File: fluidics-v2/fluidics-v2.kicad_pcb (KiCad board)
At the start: 4 copper layers, 127 x 127.2 mm, 73 parts, among them IC2 ADUM1250WSRZ-RL7, J1 PJ-063AH, J10 87832-1010, J11 0705430001, J12 87832-1010, J13 0705430001, J14 87832-1010, J15 0533980671, J16 0705430001, J17 0533980671, J18 87832-1010, J19 0705430001, J2 B6B-ZR-SM4-TF, J20 0533980671, J21 87832-1010, J22 0705430001, J24 0705430001, J25 87832-1010, J3 A-DS_15_A_KG-T4S, J4 B6B-ZR-SM4-TF, U10 LTC4311CSC6-TRPBF, U11 MAX3221, U12 CD4050BDR, U13 TC7PZ17FU, U2 Teensy4.1, U3 AP7366EA-33W5-7, U4 D24V10FX, U6 LTC4311CSC6-TRPBF, U8 LTC4311CSC6-TRPBF, U9 LTC4311CSC6-TRPBF

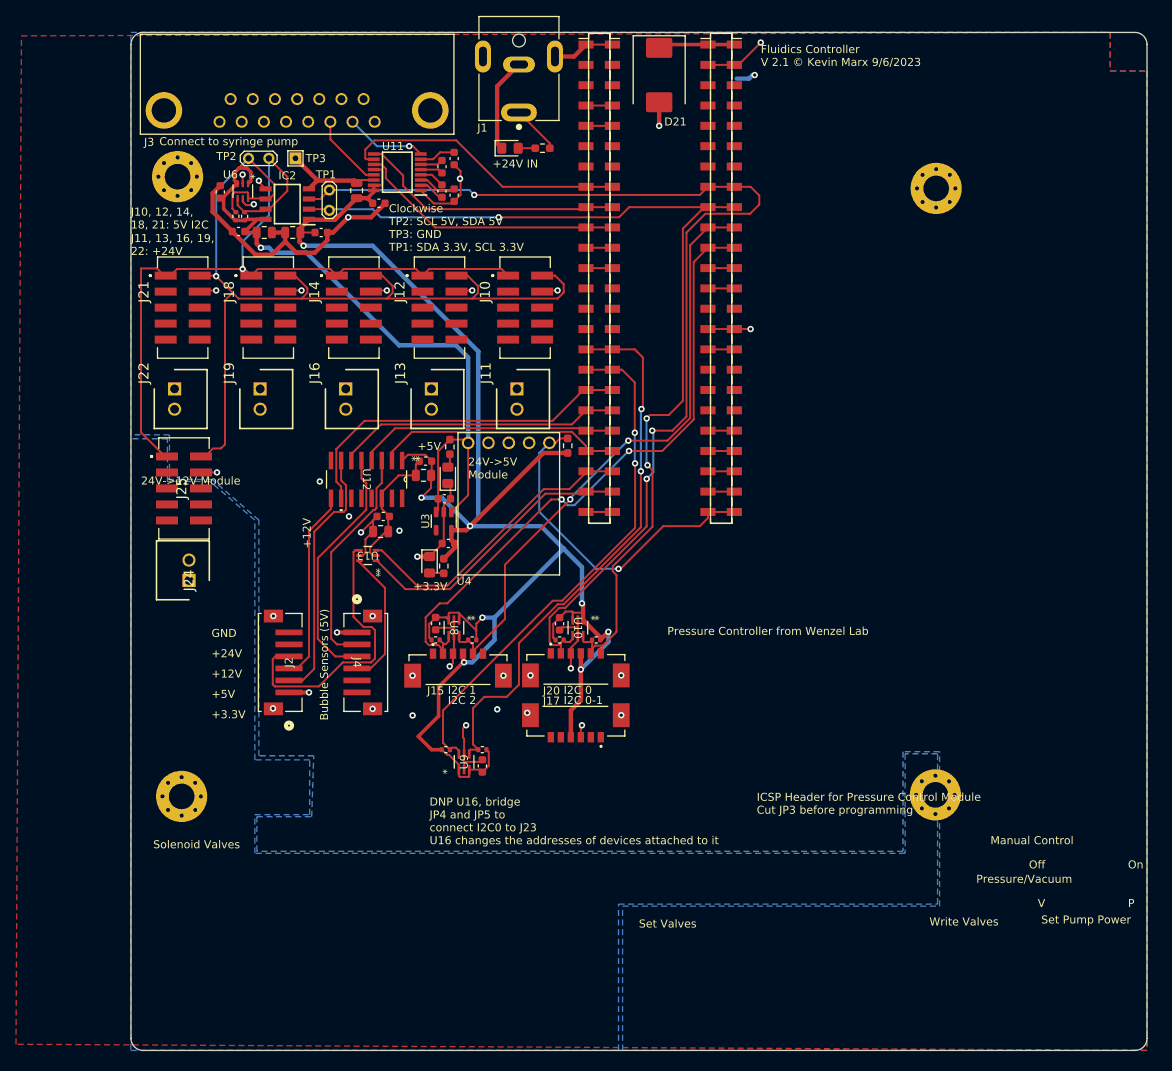
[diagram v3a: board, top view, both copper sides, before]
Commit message: @ Wire solenoid driver + status LEDs + I2C cleanup; route + connect
- Solenoid driver (U1 TPL7407): IN1-7 <- Teensy GPIO_1-7 (back-layer fanout,
  vias off the SMD pads), COM->+24V, GND->plane, OUT1-7 -> J5 screw terminal
- Add 7 solenoid status LEDs (GPIO_1-7) + COM/+24V indicator LED (0402)
- Remove LTC4311 I2C accelerators (U9/U10) - misbehaved on lightly-loaded
  buses (single-valve failure); kept passive pull-ups. Restored SCL2/SDA2
  pull-ups (R41/R42)
- Back layer: full-board GND pour (clean rectangle outline)
- Connect U1 GND and R4 (+24V power-indicator LED) to their nets

DRC: unconnected down to 5, all intentional unused-pin no-connects
(GPIO_8/9 + vestigial SPI). No shorts; vias cleared out of Teensy SMD pads.

Co-Authored-By: Claude Opus 4.8 (1M context) <noreply@anthropic.com>
@
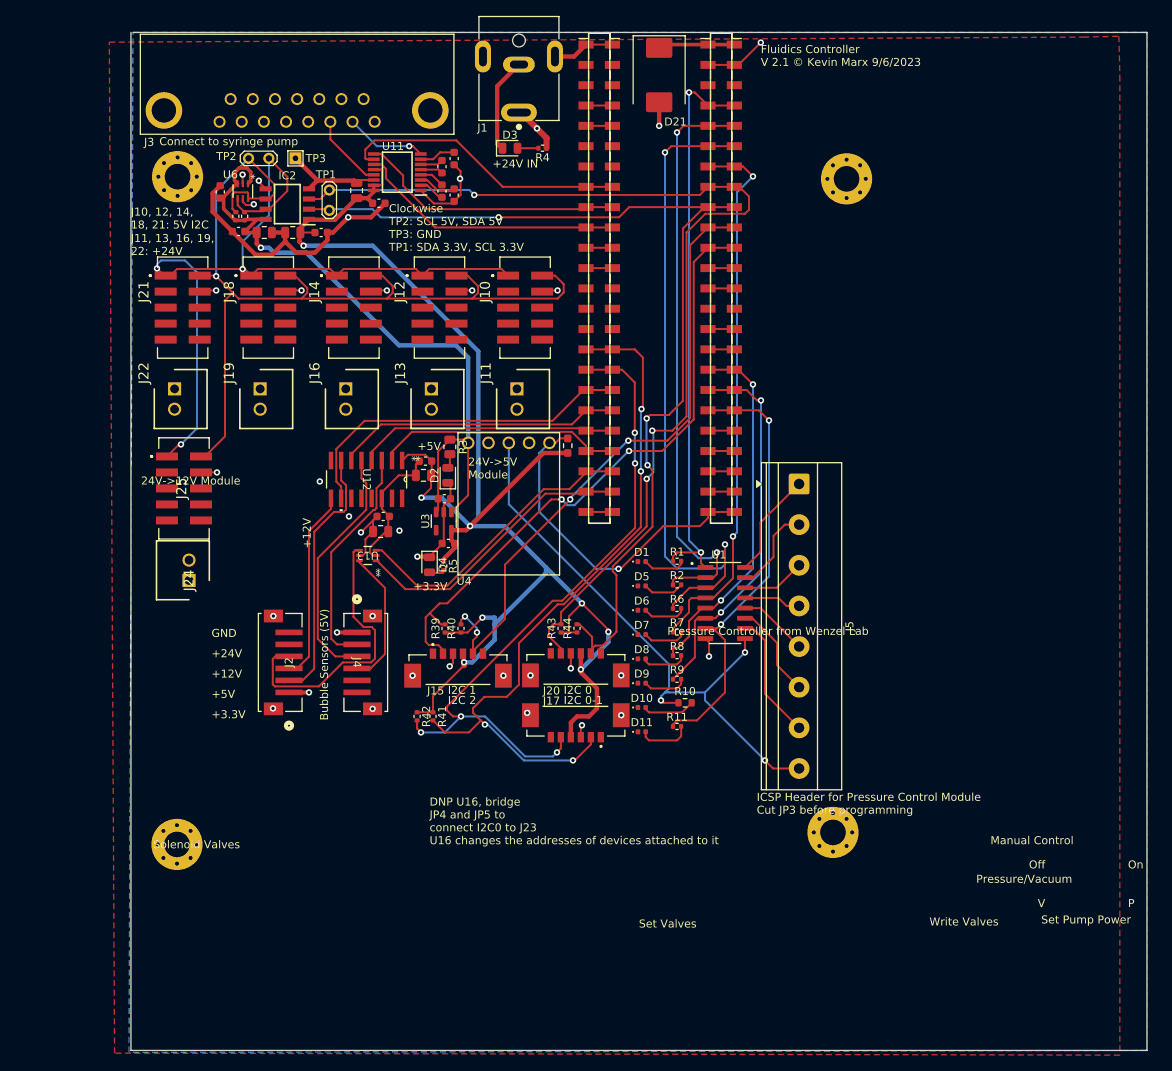
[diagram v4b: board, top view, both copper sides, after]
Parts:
- removed C12, C13, C14: 0.01u, Capacitor_SMD:C_0603_1608Metric
- removed U10, U8, U9: LTC4311CSC6-TRPBF, LTC:SOT-6_SC_LIT
- added D1: LED, LED_SMD:LED_0402_1005Metric, F.Cu at (78.6, 81.6)
- added D10: LED, LED_SMD:LED_0402_1005Metric, F.Cu at (78.6, 99.9)
- added D11: LED, LED_SMD:LED_0402_1005Metric, F.Cu at (78.6, 102.9)
- added D5: LED, LED_SMD:LED_0402_1005Metric, F.Cu at (78.6, 84.7)
- added D6: LED, LED_SMD:LED_0402_1005Metric, F.Cu at (78.6, 87.7)
- added D7: LED, LED_SMD:LED_0402_1005Metric, F.Cu at (78.6, 90.8)
- added D8: LED, LED_SMD:LED_0402_1005Metric, F.Cu at (78.6, 93.8)
- added D9: LED, LED_SMD:LED_0402_1005Metric, F.Cu at (78.6, 96.8)
- added J5: Screw_Terminal_01x08, TerminalBlock_Phoenix:TerminalBlock_Phoenix_MKDS-1,5-8-5.08_1x08_P5.08mm_Horizontal, F.Cu at (98.3, 71.9)
- added R1: 2.7K, Resistor_SMD:R_0402_1005Metric, F.Cu at (83.0, 81.6)
- added R10: 42K, Resistor_SMD:R_0603_1608Metric, F.Cu at (84.0, 99.3)
- added R11: 2.7K, Resistor_SMD:R_0402_1005Metric, F.Cu at (83.0, 102.2)
- added R2: 2.7K, Resistor_SMD:R_0402_1005Metric, F.Cu at (83.0, 84.5)
- added R6: 2.7K, Resistor_SMD:R_0402_1005Metric, F.Cu at (83.0, 87.5)
- added R7: 2.7K, Resistor_SMD:R_0402_1005Metric, F.Cu at (83.0, 90.5)
- added R8: 2.7K, Resistor_SMD:R_0402_1005Metric, F.Cu at (83.0, 93.4)
- added R9: 2.7K, Resistor_SMD:R_0402_1005Metric, F.Cu at (83.0, 96.3)
- added U1: TPL7407LDR, TPL7407LDR:SOIC127P600X175-16N, F.Cu at (89.0, 86.8)
- D2, D3, D4: footprint LED_SMD:LED_0805_2012Metric_Pad1.15x1.40mm_HandSolder -> LED_SMD:LED_0805_2012Metric
- R3: footprint Resistor_SMD:R_0603_1608Metric_Pad0.98x0.95mm_HandSolder -> Resistor_SMD:R_0805_2012Metric
- R4, R5: footprint Resistor_SMD:R_0603_1608Metric_Pad0.98x0.95mm_HandSolder -> Resistor_SMD:R_0402_1005Metric
- moved H3 13.6 mm to (102.5, 115.5)
- moved H1 11.3 mm to (104.2, 33.8)
- moved R41 7.45 mm to (52.5, 101.0), turned to -90 degrees
- moved H4 6.03 mm to (20.5, 117.0)
- moved R42 5.50 mm to (50.5, 101.0), turned to -90 degrees
- moved R44 2.80 mm to (70.5, 90.0), turned to 90 degrees
- moved R40 2.01 mm to (56.0, 90.0), turned to 90 degrees
- moved R39 1.86 mm to (54.0, 90.0), turned to 90 degrees
- moved R43 1.46 mm to (68.5, 90.0), turned to 90 degrees
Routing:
- net /GPIO_3: track 0.00 -> 82.7 mm, vias 0 -> 2
- net +24V: track 6.06 -> 79.6 mm, vias 0 -> 4
- net /GPIO_2: track 0.00 -> 73.5 mm, vias 0 -> 2
- net /GPIO_1: track 0.00 -> 70.9 mm, vias 0 -> 2
- net /GPIO_4: track 0.00 -> 68.8 mm, vias 0 -> 2
- net /GPIO_7: track 0.00 -> 56.3 mm, vias 0 -> 2
- net /GPIO_6: track 0.00 -> 47.9 mm, vias 0 -> 2
- net /GPIO_5: track 0.00 -> 46.4 mm, vias 0 -> 2
- net +3.3V: track 227.9 -> 194.5 mm
- net GND: track 160.0 -> 137.1 mm, vias 34 -> 30
- net /SCL2: track 68.9 -> 89.0 mm, vias 2 -> 4
- net /SDA2: track 65.1 -> 84.2 mm, vias 2 -> 5
- net Net-(J5-Pin_7): track 0.00 -> 15.8 mm
- net Net-(J5-Pin_1): track 0.00 -> 13.2 mm
- net Net-(J5-Pin_6): track 0.00 -> 12.0 mm
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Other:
- outline, holes or cut-outs redrawn

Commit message: @ Resize board to 94.25 x 106.25 mm; redraw front GND pour
- Shrunk Edge.Cuts from ~127x127 to 94.25 x 106.25 mm (single Rect, closed)
- All 85 footprints fit inside the new outline; all 5 zones re-poured
  (front/back GND, In1 GND plane, In2 +24V/+5V planes)
- Redrew the front F.Cu GND zone (was deleted during resize)

DRC: outline valid, no copper-to-edge or clearance errors, 5 unconnected
(expected unused-pin no-connects). Remaining are cosmetic: silk-edge-clearance
(20, silk now near the smaller edge) + inherited silk/courtyard/lib warnings.

Co-Authored-By: Claude Opus 4.8 (1M context) <noreply@anthropic.com>
@
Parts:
- moved C15 94.6 mm to (140.2, 42.0)
- moved C16 94.6 mm to (148.1, 40.4)
- moved C17 94.6 mm to (148.1, 37.4)
- moved C19 94.6 mm to (149.6, 40.9)
- moved C2 94.6 mm to (148.9, 84.5)
- moved C20 94.6 mm to (149.6, 36.4)
- moved C23 94.6 mm to (145.8, 76.0)
- moved D1 94.6 mm to (173.1, 86.7)
- moved D10 94.6 mm to (173.1, 105.0)
- moved D11 94.6 mm to (173.1, 108.0)
- moved D2 94.6 mm to (148.8, 76.0)
- moved D3 94.6 mm to (156.6, 35.1)
- moved D4 94.6 mm to (146.5, 87.1)
- moved D5 94.6 mm to (173.1, 89.8)
- moved D6 94.6 mm to (173.1, 92.8)
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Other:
- board size 127 x 127.2 mm -> 94 x 106 mm

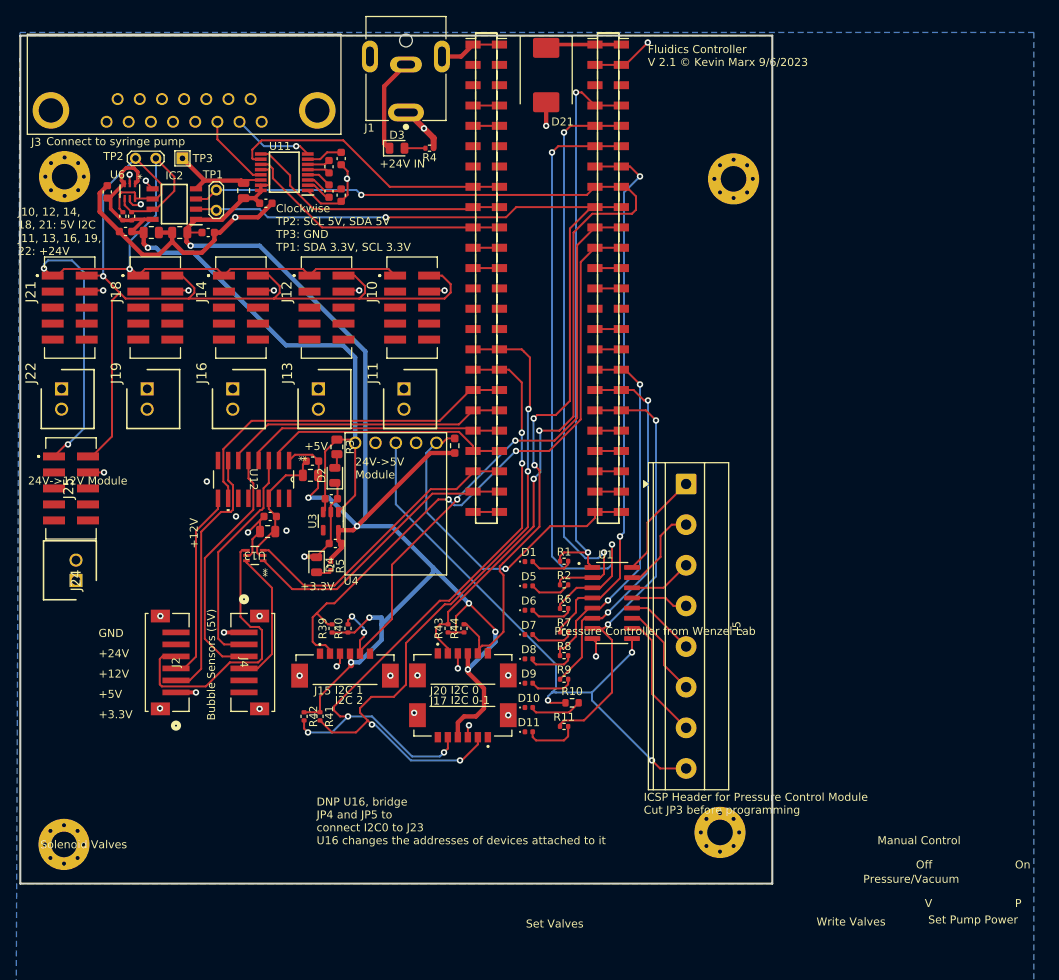
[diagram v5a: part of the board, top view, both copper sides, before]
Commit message: Trim board: remove D1/D5-D8/R1/R2/R6-R8/H1, add connector J6
PCB + root schematic + solenoid_driver sheet edits (GUI-driven).
Footprints 85 -> 75. Removed diodes D1/D5-D8, resistors R1/R2/R6-R8,
mounting hole H1; added connector J6. Schematic/PCB in parity
(kicad-cli drc: schematic_parity 0). Remaining DRC items are the
inherited-from-upstream cosmetic set (silk_over_copper, malformed
_courtyard, lib_footprint_mismatch) plus 5 intentional no-connects
and 1 dangling track.

Co-Authored-By: Claude Opus 4.8 (1M context) <noreply@anthropic.com>
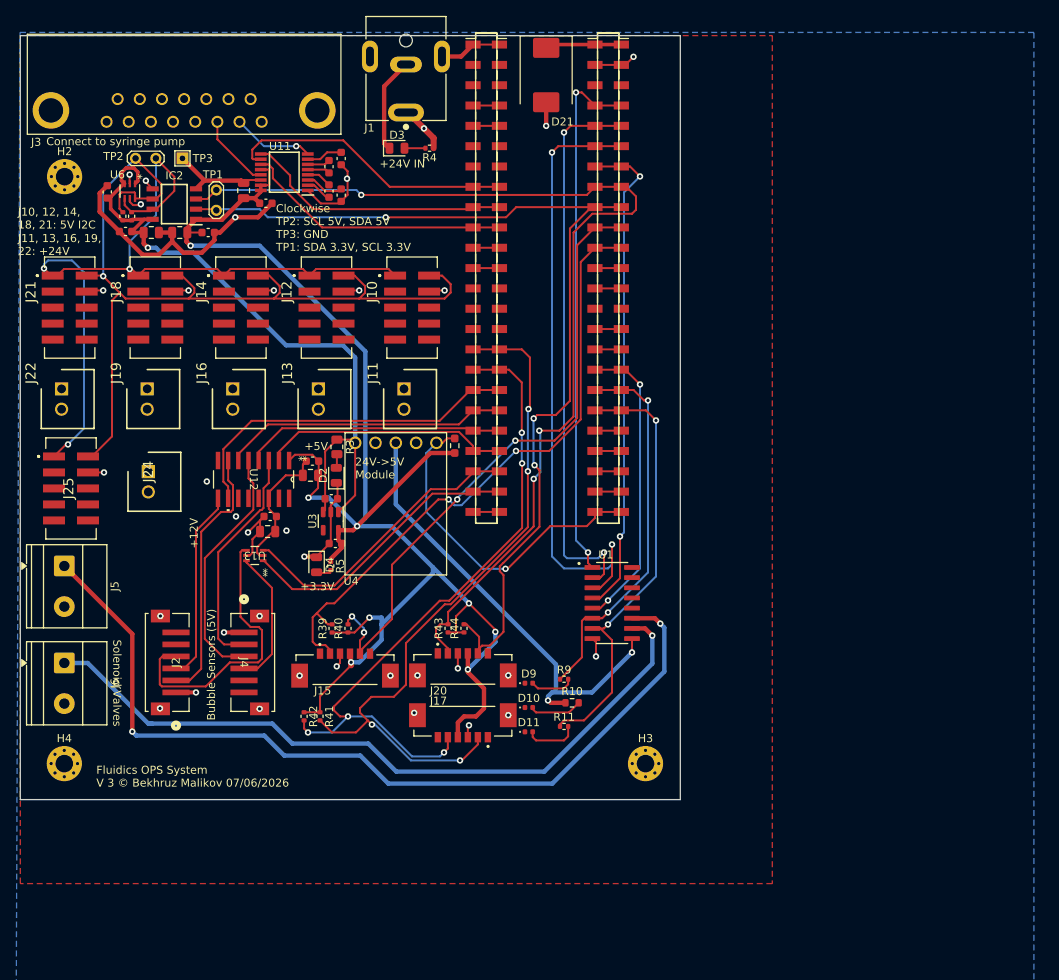
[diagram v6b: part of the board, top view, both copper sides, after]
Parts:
- removed D1, D5, D6, D7, D8: LED, LED_SMD:LED_0402_1005Metric
- removed H1: MountingHole_Pad, MountingHole:MountingHole_3.2mm_M3_Pad_Via
- removed R1, R2, R6, R7, R8: 2.7K, Resistor_SMD:R_0402_1005Metric
- added J6: Screw_Terminal_01x02, TerminalBlock_Phoenix:TerminalBlock_Phoenix_MKDS-1,5-2-5.08_1x02_P5.08mm_Horizontal, F.Cu at (115.0, 99.4)
- H2, H3, H4: footprint MountingHole:MountingHole_3.2mm_M3_Pad_Via -> MountingHole:MountingHole_2.2mm_M2_Pad_Via
- J5: value Screw_Terminal_01x08 -> Screw_Terminal_01x02; footprint TerminalBlock_Phoenix:TerminalBlock_Phoenix_MKDS-1,5-8-5.08_1x08_P5.08mm_Horizontal -> TerminalBlock_Phoenix:TerminalBlock_Phoenix_MKDS-1,5-2-5.08_1x02_P5.08mm_Horizontal
- moved J5 78.4 mm to (115.0, 87.3)
- moved J24 16.3 mm to (125.5, 75.5), turned to -90 degrees
- moved H3 12.7 mm to (187.7, 112.0)
- moved H4 10.1 mm to (115.0, 112.0)
- moved D2 0.18 mm to (149.0, 76.0)
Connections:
- J5 pad 2: Net-(J5-Pin_2) -> +24V
- U1 pad 10: Net-(J5-Pin_7) -> Net-(J6-Pin_1)
- U1 pad 11: Net-(J5-Pin_6) -> Net-(J5-Pin_1)
- U1 pad 12: Net-(J5-Pin_5) -> unconnected-(U1-OUT5-Pad12)
- U1 pad 13: Net-(J5-Pin_4) -> unconnected-(U1-OUT4-Pad13)
- U1 pad 14: Net-(J5-Pin_3) -> unconnected-(U1-OUT3-Pad14)
- U1 pad 15: Net-(J5-Pin_2) -> unconnected-(U1-OUT2-Pad15)
- U1 pad 16: Net-(J5-Pin_1) -> unconnected-(U1-OUT1-Pad16)
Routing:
- net Net-(J5-Pin_1): track 13.2 -> 109.2 mm, vias 0 -> 2
- net Net-(J6-Pin_1): track 0.00 -> 91.3 mm, vias 0 -> 1
- net +24V: track 79.6 -> 62.8 mm, vias 4 -> 3
- net Net-(J5-Pin_7): track 15.8 -> 0.00 mm
- net Net-(J5-Pin_6): track 12.0 -> 0.00 mm
- net Net-(J5-Pin_2): track 11.1 -> 0.00 mm
- net /GPIO_5: track 46.4 -> 37.4 mm
- net Net-(J5-Pin_5): track 8.76 -> 0.00 mm
- net Net-(J5-Pin_3): track 7.93 -> 0.00 mm
- net Net-(J5-Pin_4): track 7.18 -> 0.00 mm
- net /GPIO_4: track 68.8 -> 61.9 mm
- net Net-(D8-A): track 5.68 -> 0.00 mm
- net Net-(D7-A): track 5.48 -> 0.00 mm
- net Net-(D6-A): track 5.45 -> 0.00 mm
- net /GPIO_3: track 82.7 -> 77.3 mm
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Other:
- board size 94 x 106 mm -> 82.5 x 95.5 mm
- board text added: "Fluidics OPS System V 3 © Bekhruz Malikov 07/06/2026"
- board text removed: "+24V"
- board text removed: "24V->12V Module"
- board text removed: "DNP U16, bridge JP4 and JP5 to connect I2C0 to J23 U16 changes the addresses of devices attached to it"
- board text removed: "Fluidics Controller V 2.1 © Kevin Marx 9/6/2023"
- board text removed: "GND"
- board text removed: "I2C 0"
- board text removed: "I2C 0-1"
- board text removed: "I2C 1"
- board text removed: "I2C 2"
- board text removed: "ICSP Header for Pressure Control Module Cut JP3 before programming"
- board text removed: "Manual Control"
- board text removed: "Off"
- board text removed: "On"
- board text removed: "P"
- board text removed: "Pressure Controller from Wenzel Lab"
- board text removed: "Pressure/Vacuum"
- board text removed: "Set Pump Power"
- board text removed: "Set Valves"
- board text removed: "V"
- board text removed: "Write Valves"

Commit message: Place Cephla logo on F.SilkS (30%), add logo footprints; i2c sheet edit
- Placed bitmap2component logo (ref G***) on front silkscreen, scaled
  to 30% of original -> 12.40 x 4.88 mm; footprints 75 -> 76.
- Add logo source footprints: ImageCephlaCompanyPCB.kicad_mod (full)
  + _30pct (placed variant). Abandoned Attempt2/3 left untracked.
- i2c.kicad_sch: non-component edit (wiring/label), saved from GUI.

Co-Authored-By: Claude Opus 4.8 (1M context) <noreply@anthropic.com>
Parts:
- added G***: LOGO, ImageCephlaCompanyPCB_30pct, F.Cu at (125.0, 114.0)
- moved H3 2.21 mm to (185.5, 112.5)
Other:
- board text added: "Fluidics OPS System V3 © Bekhruz Malikov 07/06/2026"
- board text removed: "Fluidics OPS System V 3 © Bekhruz Malikov 07/06/2026"
- board text removed: "J10, 12, 14, 18, 21: 5V I2C"
- board text removed: "J11, 13, 16, 19, 22: +24V"
